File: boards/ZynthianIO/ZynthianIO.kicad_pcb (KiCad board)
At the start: 2 copper layers, 88.9 x 78.7 mm, 25 parts, among them J1 Raspberry_Pi_2_3, J2 GPIO, U1 MCP23017_SP, U2 6N138, U3 74LS14

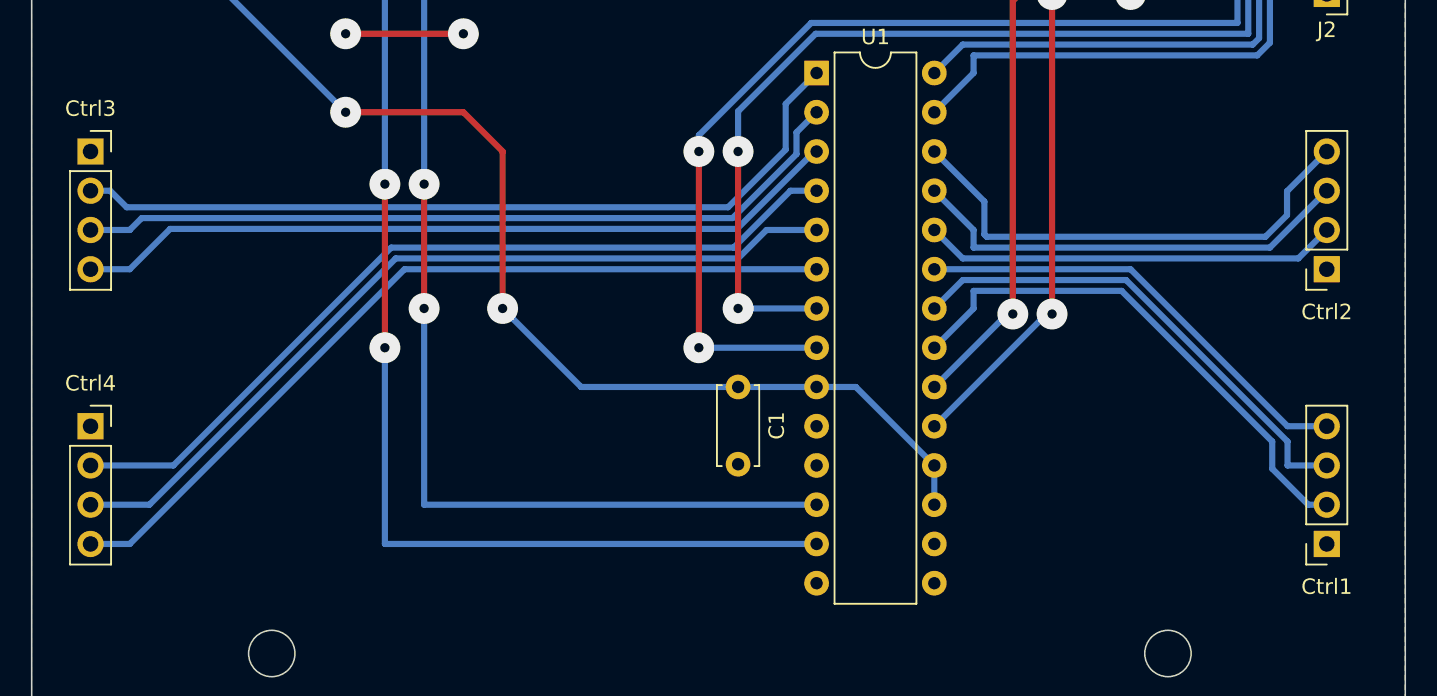
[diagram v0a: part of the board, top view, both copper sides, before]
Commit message: Removed temporary and local KiCAD files
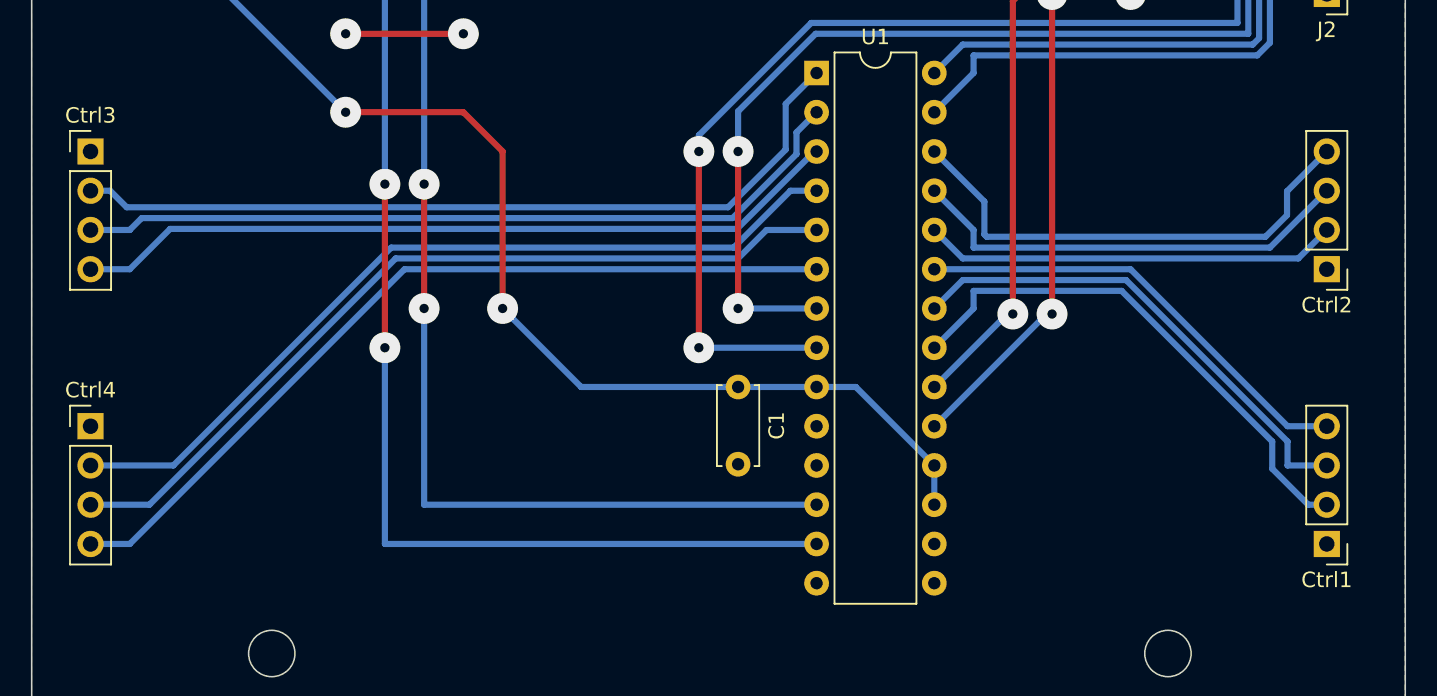
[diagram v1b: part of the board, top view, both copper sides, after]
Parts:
- Ctrl1, Ctrl2, Ctrl3, Ctrl4: footprint Connector_PinSocket_2.54mm:PinSocket_1x04_P2.54mm_Vertical -> Connector_PinHeader_2.54mm:PinHeader_1x04_P2.54mm_Vertical

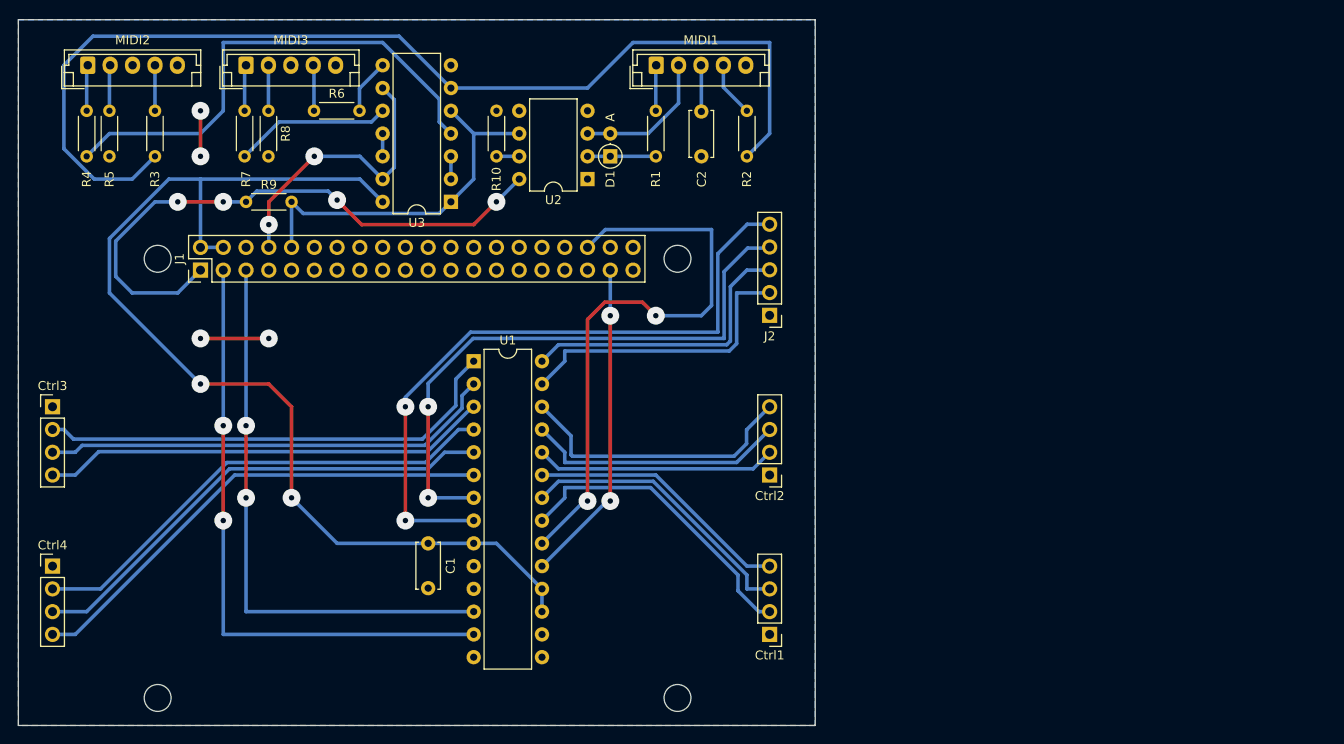
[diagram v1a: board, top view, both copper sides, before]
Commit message: Updated IO expander board with Raspberry HAT template PCB design
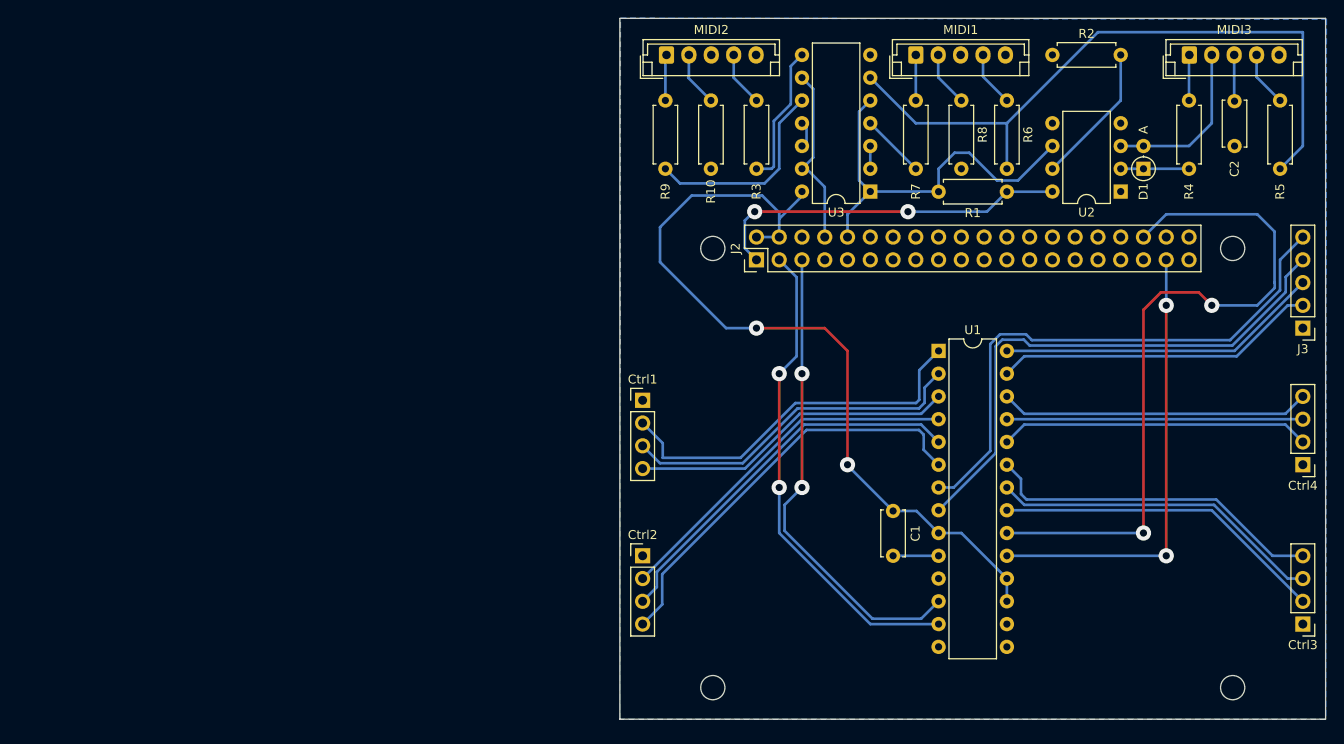
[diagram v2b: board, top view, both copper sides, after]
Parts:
- removed J1: Raspberry_Pi_2_3, Connector_PinHeader_2.54mm:PinHeader_2x20_P2.54mm_Vertical
- added J3: GPIO, Connector_PinHeader_2.54mm:PinHeader_1x05_P2.54mm_Vertical, F.Cu at (229.7, 108.1)
- added MH1: MountingHole_2.7mm_M2.5, MountingHole:MountingHole_2.7mm_M2.5, F.Cu at (163.8, 99.2)
- added MH2: MountingHole_2.7mm_M2.5, MountingHole:MountingHole_2.7mm_M2.5, F.Cu at (221.8, 99.2)
- added MH3: MountingHole_2.7mm_M2.5, MountingHole:MountingHole_2.7mm_M2.5, F.Cu at (163.8, 148.2)
- added MH4: MountingHole_2.7mm_M2.5, MountingHole:MountingHole_2.7mm_M2.5, F.Cu at (221.8, 148.2)
- Ctrl1: value Ctrl-1 -> Ctrl-3
- Ctrl2: value Ctrl-2 -> Ctrl-4
- Ctrl3: value Ctrl-3 -> Ctrl-1
- Ctrl4: value Ctrl-4 -> Ctrl-2
- J2: value GPIO -> Raspberry_Pi_2_3; footprint Connector_PinHeader_2.54mm:PinHeader_1x05_P2.54mm_Vertical -> Connector_PinHeader_2.54mm:PinHeader_2x20_P2.54mm_Vertical
- MIDI1: value MIDI_IN -> MIDI_THRU
- MIDI2: value MIDI_THRU -> MIDI_OUT
- MIDI3: value MIDI_OUT -> MIDI_IN
- R1, R5: value 100 -> 220; footprint Resistor_THT:R_Axial_DIN0204_L3.6mm_D1.6mm_P5.08mm_Horizontal -> Resistor_THT:R_Axial_DIN0207_L6.3mm_D2.5mm_P7.62mm_Horizontal
- R10, R9: value 220 -> 100; footprint Resistor_THT:R_Axial_DIN0204_L3.6mm_D1.6mm_P5.08mm_Horizontal -> Resistor_THT:R_Axial_DIN0207_L6.3mm_D2.5mm_P7.62mm_Horizontal
- R2, R3, R4, R6, R7, R8: footprint Resistor_THT:R_Axial_DIN0204_L3.6mm_D1.6mm_P5.08mm_Horizontal -> Resistor_THT:R_Axial_DIN0207_L6.3mm_D2.5mm_P7.62mm_Horizontal
- moved Ctrl3 141.6 mm to (229.7, 141.1), turned to 180 degrees
- moved Ctrl4 140.0 mm to (229.7, 123.3), turned to 180 degrees
- moved R5 130.6 mm to (227.1, 82.7)
- moved R4 123.0 mm to (217.0, 82.7)
- moved MIDI3 105.3 mm to (217.0, 77.6)
- moved R6 77.3 mm to (196.6, 82.7), turned to -90 degrees
- moved R8 77.3 mm to (191.6, 82.7)
- moved R7 74.9 mm to (186.5, 82.7)
- moved R3 67.1 mm to (168.7, 82.7)
- moved MIDI2 64.6 mm to (158.7, 77.6)
- moved D1 59.5 mm to (211.9, 90.3)
- moved U2 59.5 mm to (209.3, 92.8)
- moved C2 59.5 mm to (222.0, 82.7)
- moved C1 52.0 mm to (183.9, 128.5)
- moved U1 51.9 mm to (189.0, 110.6)
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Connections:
- C2 pad 1: Net-(MIDI1-Pin_3) -> Net-(MIDI3-Pin_3)
- J2 pad 1: GND -> +3V3
- J2 pad 2: /GPA6 -> +5V
- J2 pad 3: /GPA7 -> /SDA
- J2 pad 4: /GPB6 -> +5V
- J2 pad 5: /GPB7 -> /SCK
- MIDI1 pad 2: Net-(D1-A) -> Net-(MIDI1-Pin_2)
- MIDI1 pad 3: Net-(MIDI1-Pin_3) -> GND
- MIDI3 pad 2: Net-(MIDI3-Pin_2) -> Net-(D1-A)
- MIDI3 pad 3: GND -> Net-(MIDI3-Pin_3)
- R1 pad 1: Net-(MIDI1-Pin_1) -> +3V3
- R1 pad 2: Net-(D1-K) -> /MIDI_IN
- R10 pad 1: GND -> Net-(MIDI2-Pin_2)
- R10 pad 2: Net-(U2-VO1) -> GND
- R2 pad 1: Net-(MIDI1-Pin_4) -> GND
- R2 pad 2: Net-(R2-Pad2) -> Net-(U2-VO1)
- R3 pad 2: Net-(R2-Pad2) -> Net-(R3-Pad2)
- R4 pad 1: Net-(MIDI2-Pin_1) -> Net-(MIDI3-Pin_1)
- R4 pad 2: Net-(R4-Pad2) -> Net-(D1-K)
- R5 pad 1: Net-(MIDI2-Pin_2) -> Net-(MIDI3-Pin_4)
- R5 pad 2: GND -> Net-(R5-Pad2)
- R6 pad 1: Net-(MIDI3-Pin_4) -> Net-(MIDI1-Pin_4)
- R6 pad 2: Net-(R6-Pad2) -> Net-(R5-Pad2)
- R7 pad 1: Net-(MIDI3-Pin_1) -> Net-(MIDI1-Pin_1)
- R8 pad 1: Net-(MIDI3-Pin_2) -> Net-(MIDI1-Pin_2)
- R9 pad 1: +3.3V -> Net-(MIDI2-Pin_1)
- R9 pad 2: /MIDI_IN -> Net-(R9-Pad2)
- U1 pad 1: Net-(Ctrl3-Pin_2) -> Net-(Ctrl1-Pin_2)
- U1 pad 2: Net-(Ctrl3-Pin_3) -> Net-(Ctrl1-Pin_3)
- U1 pad 21: Net-(Ctrl1-Pin_2) -> Net-(Ctrl3-Pin_2)
- U1 pad 22: Net-(Ctrl1-Pin_3) -> Net-(Ctrl3-Pin_3)
- U1 pad 23: Net-(Ctrl1-Pin_4) -> Net-(Ctrl3-Pin_4)
- U1 pad 24: Net-(Ctrl2-Pin_2) -> Net-(Ctrl4-Pin_2)
- U1 pad 25: Net-(Ctrl2-Pin_3) -> Net-(Ctrl4-Pin_3)
- U1 pad 26: Net-(Ctrl2-Pin_4) -> Net-(Ctrl4-Pin_4)
- U1 pad 3: Net-(Ctrl3-Pin_4) -> Net-(Ctrl1-Pin_4)
- U1 pad 4: Net-(Ctrl4-Pin_2) -> Net-(Ctrl2-Pin_2)
- U1 pad 5: Net-(Ctrl4-Pin_3) -> Net-(Ctrl2-Pin_3)
- U1 pad 6: Net-(Ctrl4-Pin_4) -> Net-(Ctrl2-Pin_4)
- U2 pad 8: +3.3V -> +3V3
- U3 pad 10: Net-(R7-Pad2) -> Net-(R9-Pad2)
- U3 pad 4: Net-(R4-Pad2) -> Net-(R7-Pad2)
- U3 pad 6: Net-(R2-Pad2) -> Net-(R5-Pad2)
- U3 pad 8: Net-(R6-Pad2) -> Net-(R3-Pad2)
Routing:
- net Net-(R2-Pad2): track 120.3 -> 0.00 mm
- net Net-(R5-Pad2): track 0.00 -> 75.9 mm
- net +3.3V: track 66.2 -> 0.00 mm, vias 4 -> 0
- net Net-(R4-Pad2): track 56.1 -> 0.00 mm
- net +3V3: track 0.00 -> 40.6 mm, vias 0 -> 2
- net +5V: track 120.9 -> 92.4 mm
- net Net-(R9-Pad2): track 0.00 -> 22.7 mm
- net Net-(Ctrl4-Pin_3): track 54.4 -> 33.0 mm
- net Net-(Ctrl4-Pin_4): track 54.4 -> 34.6 mm
- net Net-(Ctrl4-Pin_2): track 54.4 -> 34.6 mm
- net Net-(R3-Pad2): track 0.00 -> 15.8 mm
- net Net-(Ctrl3-Pin_2): track 52.8 -> 37.2 mm
- net /SDA: track 68.6 -> 54.1 mm
- net Net-(Ctrl2-Pin_4): track 32.1 -> 46.6 mm
- net /INTB: track 36.4 -> 50.8 mm
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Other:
- board size 88.9 x 78.7 mm -> 78.7 x 78.2 mm

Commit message: Fixing several layout issues due to KiCAD 7.0.2/Linux update
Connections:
- net +3V3 renamed +3.3V
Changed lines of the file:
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@@
   (net 1 "GND")
   (net 2 "+5V")
-  (net 3 "+3V3")
+  (net 3 "+3.3V")
   (net 4 "Net-(MIDI3-Pin_3)")
   (net 5 "Net-(Ctrl1-Pin_2)")
@@
       (stroke (width 0.1) (type solid)) (layer "F.Fab"))
     (pad "1" thru_hole rect (at 0 0 90) (size 1.7 1.7) (drill 1) (layers "*.Cu" "*.Mask")
-      (net 3 "+3V3") (pinfunction "3V3") (pintype "power_in"))
+      (net 3 "+3.3V") (pinfunction "3V3") (pintype "power_in"))
     (pad "2" thru_hole oval (at 2.54 0 90) (size 1.7 1.7) (drill 1) (layers "*.Cu" "*.Mask")
       (net 2 "+5V") (pinfunction "5V") (pintype "power_in"))
@@
     (property "ki_keywords" "diode")
     (attr through_hole)
-    (fp_text reference "D1" (at -2.54 0 90) (layer "F.SilkS")
+    (fp_text reference "D1" (at 1.27 -2.326371 90) (layer "F.SilkS")
         (effects (font (size 1 1) (thickness 0.15)))
     )
@@
       (net 62 "Net-(U2-VO1)") (pinfunction "VO1") (pintype "passive"))
     (pad "8" thru_hole oval (at 7.62 0 180) (size 1.6 1.6) (drill 0.8) (layers "*.Cu" "*.Mask")
-      (net 3 "+3V3") (pinfunction "VCC") (pintype "passive"))
+      (net 3 "+3.3V") (pinfunction "VCC") (pintype "passive"))
     (model "${KICAD6_3DMODEL_DIR}/Package_DIP.3dshapes/DIP-8_W7.62mm.wrl"
       (offset (xyz 0 0 0))
@@
       (stroke (width 0.1) (type solid)) (layer "F.Fab"))
     (pad "1" thru_hole circle (at 0 0 180) (size 1.6 1.6) (drill 0.8) (layers "*.Cu" "*.Mask")
-      (net 3 "+3V3") (pintype "passive"))
+      (net 3 "+3.3V") (pintype "passive"))
     (pad "2" thru_hole oval (at 7.62 0 180) (size 1.6 1.6) (drill 0.8) (layers "*.Cu" "*.Mask")
       (net 24 "/MIDI_IN") (pintype "passive"))
@@
   (segment (start 222.00868 77.58868) (end 222.00868 82.70868) (width 0.3) (layer "B.Cu") (net 4))
   (segment (start 186.510081 116.42868) (end 173.043096 116.42868) (width 0.3) (layer "B.Cu") (net 5))
+  (segment (start 158.25091 122.53868) (end 166.933096 122.53868) (width 0.3) (layer "B.Cu") (net 5))
   (segment (start 189.02868 110.60868) (end 186.872751 112.764609) (width 0.3) (layer "B.Cu") (net 5))
   (segment (start 186.872751 112.764609) (end 186.872751 116.06601) (width 0.3) (layer "B.Cu") (net 5))
   (segment (start 158.25091 120.90091) (end 156.00868 118.65868) (width 0.3) (layer "B.Cu") (net 5))
-  (segment (start 166.933096 122.53868) (end 158.25091 122.53868) (width 0.3) (layer "B.Cu") (net 5))
   (segment (start 186.872751 116.06601) (end 186.510081 116.42868) (width 0.3) (layer "B.Cu") (net 5))
   (segment (start 158.25091 122.53868) (end 158.25091 120.90091) (width 0.3) (layer "B.Cu") (net 5))
@@
   (segment (start 172.53868 78.83868) (end 173.78868 77.58868) (width 0.3) (layer "B.Cu") (net 63))
   (segment (start 196.64868 90.28868) (end 196.64868 85.20868) (width 0.3) (layer "B.Cu") (net 64))
+  (segment (start 229.66868 87.74868) (end 227.12868 90.28868) (width 0.3) (layer "B.Cu") (net 64))
+  (segment (start 181.40868 80.12868) (end 186.48868 85.20868) (width 0.3) (layer "B.Cu") (net 64))
   (segment (start 229.66868 75.04868) (end 229.66868 87.74868) (width 0.3) (layer "B.Cu") (net 64))
-  (segment (start 181.40868 80.12868) (end 186.48868 85.20868) (width 0.3) (layer "B.Cu") (net 64))
-  (segment (start 229.66868 87.74868) (end 227.12868 90.28868) (width 0.3) (layer "B.Cu") (net 64))
   (segment (start 186.48868 85.20868) (end 196.64868 85.20868) (width 0.3) (layer "B.Cu") (net 64))
   (segment (start 196.64868 85.20868) (end 206.80868 75.04868) (width 0.3) (layer "B.Cu") (net 64))
@@
   (segment (start 181.40868 85.20868) (end 186.48868 90.28868) (width 0.3) (layer "B.Cu") (net 65))
   (segment (start 171.24868 90.28868) (end 171.24868 85.20868) (width 0.3) (layer "B.Cu") (net 66))
+  (segment (start 161.08868 91.918981) (end 169.618379 91.918981) (width 0.3) (layer "B.Cu") (net 66))
   (segment (start 171.24868 85.20868) (end 173.78868 82.66868) (width 0.3) (layer "B.Cu") (net 66))
+  (segment (start 160.178981 91.918981) (end 161.08868 91.918981) (width 0.3) (layer "B.Cu") (net 66))
   (segment (start 158.54868 90.28868) (end 160.178981 91.918981) (width 0.3) (layer "B.Cu") (net 66))
   (segment (start 169.618379 91.918981) (end 171.24868 90.28868) (width 0.3) (layer "B.Cu") (net 66))
-  (segment (start 160.178981 91.918981) (end 169.618379 91.918981) (width 0.3) (layer "B.Cu") (net 66))
   (segment (start 181.40868 90.28868) (end 181.40868 87.74868) (width 0.3) (layer "B.Cu") (net 71))
   (segment (start 174.29868 87.74868) (end 174.29868 85.20868) (width 0.3) (layer "B.Cu") (net 72))
